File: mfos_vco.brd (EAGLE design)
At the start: 100 x 80.8 mm, 60 parts, among them IC1 TL072P, IC2 TL072P, IC3 TL072P, IC4 LM394N, U1 POWER, U2 2N5457

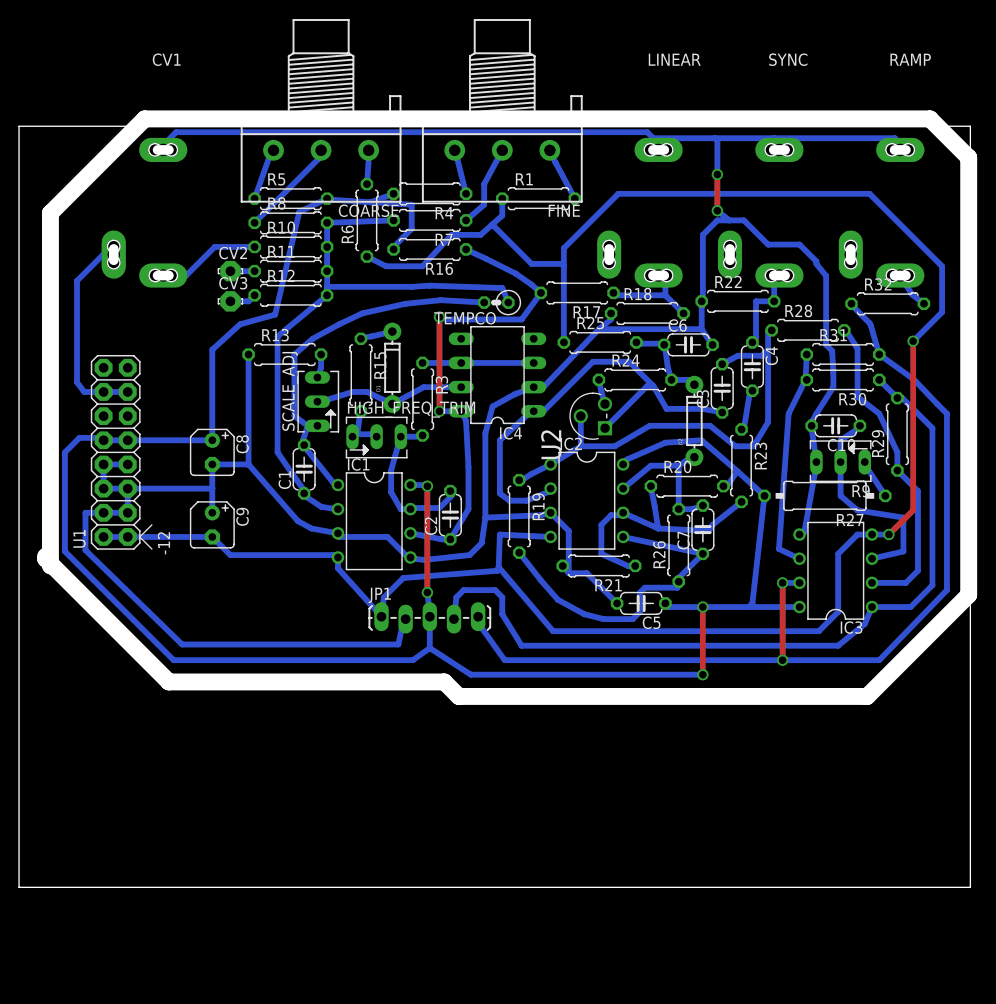
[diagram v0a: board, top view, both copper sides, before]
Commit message: thicker traces and fewer jumps
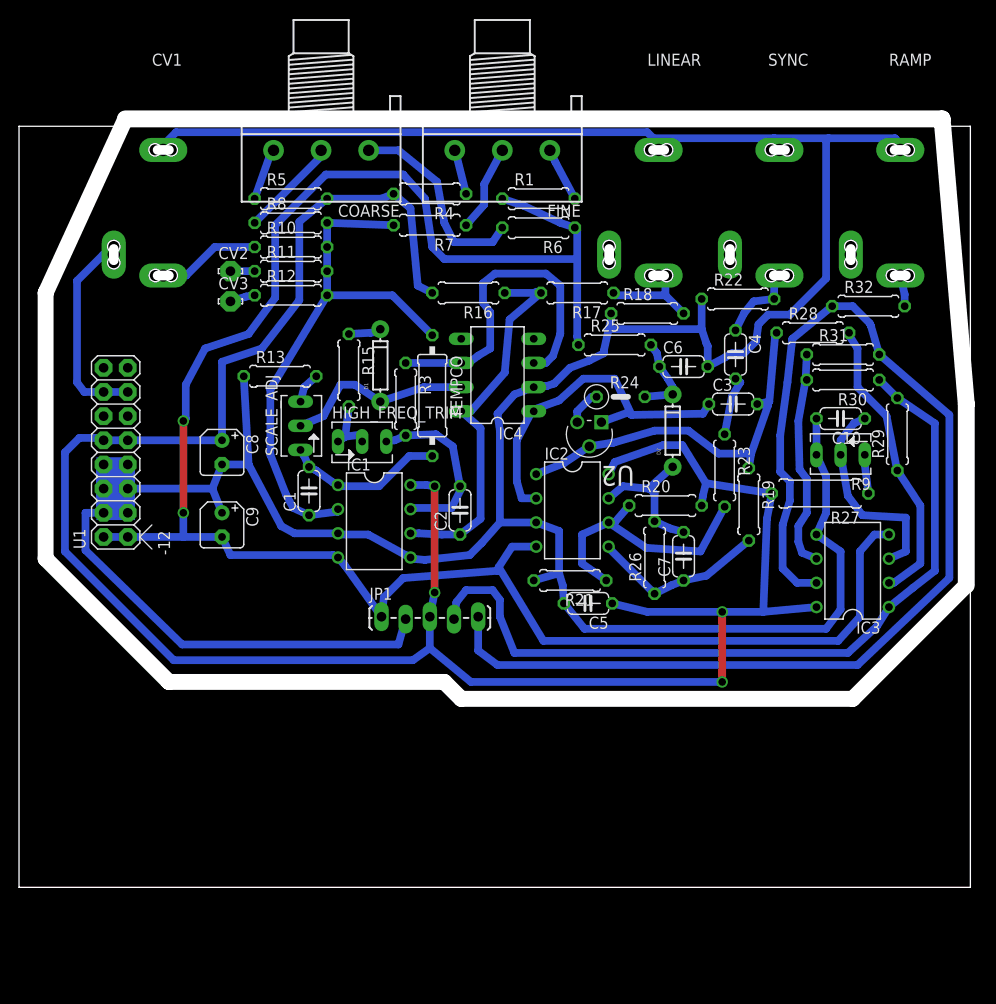
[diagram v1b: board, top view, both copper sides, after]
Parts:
- R24: device rcl:0207/7 -> rcl:0207/5V
- R27: device rcl:0309/12 -> rcl:0309/10
- TEMPCO: device rcl:0207/2V -> rcl:0309/12
- moved R19 24.2 mm to (76.7, 40.3)
- moved R6 18.1 mm to (54.6, 69.3), turned to 180 degrees
- moved TEMPCO 11.9 mm to (43.4, 51.7), turned to 270 degrees
- moved R16 6.12 mm to (47.2, 62.5)
- moved C5 5.59 mm to (59.8, 29.8)
- moved U2 4.46 mm to (58.7, 46.4), turned to 180 degrees
- moved C7 3.45 mm to (69.8, 34.8)
- moved R21 3.41 mm to (57.9, 32.3)
- moved SCALE_ADJ 3.10 mm to (29.6, 48.5)
- moved R20 3.06 mm to (67.9, 40.1)
- moved R26 2.84 mm to (66.8, 34.7)
- moved D2 2.50 mm to (68.7, 48.0)
- moved C6 2.34 mm to (69.8, 54.7)
- moved R13 2.34 mm to (27.4, 53.7)
- moved C1 2.34 mm to (30.5, 41.7)
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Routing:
- net N$35: track 99.2 -> 126.6 mm, vias 2 -> 0
- net N$12: track 11.7 -> 36.3 mm
- net N$9: track 38.3 -> 16.9 mm
- net GND: track 332.1 -> 350.7 mm, vias 2 -> 0
- net N$1: track 3.65 -> 20.9 mm
- net +12V: track 220.4 -> 237.6 mm
- net N$22: track 35.2 -> 18.5 mm
- net -12V: track 222.9 -> 206.4 mm
- net N$13: track 51.8 -> 40.8 mm, vias 2 -> 0
- net N$23: track 48.3 -> 37.5 mm
- net N$21: track 48.8 -> 41.8 mm
- net N$10: track 62.9 -> 57.4 mm
- net N$8: track 16.0 -> 19.9 mm
- net N$31: track 33.6 -> 31.3 mm
- net N$24: track 4.43 -> 6.41 mm
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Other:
- outline, holes or cut-outs redrawn

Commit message: molex
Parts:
- removed C8, C9: 10uF, rcl:B45181A
- removed JP1: (no value), SparkFun-Connectors:1X05_LOCK_LONGPADS
- removed U1: POWER, eurorack:POWER_16
- added C11, C12: 10u, rcl:B45181A
- added C13, C14: 100n, rcl:C050-024X044
- added PWR1: POWER, eurorack:POWER_16
- added U$1, U$2: FB, adafruit:FB
- added X1: 22-23-2051, con-molex:22-23-2051
- CV2, CV3: value LSP10 -> 22-23-2021; device solpad:LSP10 -> con-molex:22-23-2021
- R26: device rcl:0207/7 -> rcl:0309/10
- R27: device rcl:0309/10 -> rcl:0207/10
- moved CV1 115.0 mm to (93.7, 1.02), turned to 180 degrees
- moved RAMP 106.5 mm to (16.3, 1.02), turned to 180 degrees
- moved SYNC 91.4 mm to (29.0, 1.02), turned to 180 degrees
- moved R32 85.3 mm to (14.6, 19.9), turned to 180 degrees
- moved COARSE 84.2 mm to (72.1, 3.56), turned to 0 degrees
- moved R29 82.0 mm to (11.6, 33.4), turned to 270 degrees
- moved LINEAR 81.6 mm to (41.7, 1.02), turned to 180 degrees
- moved R5 79.0 mm to (75.3, 8.64), turned to 180 degrees
- moved R31 76.0 mm to (17.3, 25.0), turned to 180 degrees
- moved R8 75.0 mm to (75.3, 11.2), turned to 180 degrees
- moved FINE 73.9 mm to (53.1, 3.56), turned to 0 degrees
- moved R30 73.9 mm to (17.3, 27.7), turned to 0 degrees
- moved CV2 73.5 mm to (82.5, 22.9), turned to 90 degrees
- moved IC3 72.8 mm to (16.3, 47.8), turned to 270 degrees
- moved R28 72.3 mm to (20.4, 22.7), turned to 180 degrees
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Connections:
- new net N$38: PWR1.10, PWR1.9, U$1.P$1
- new net N$39: PWR1.1, PWR1.2, U$2.P$1
- net +12V: now also C11.+, C13.1, U$1.P$2, X1.3; no longer C8.+, JP1.3, U1.10, U1.9
- net -12V: now also C12.-, C14.2, U$2.P$2, X1.1; no longer C9.-, JP1.1, U1.1, U1.2
- net GND: now also CV2.2, CV3.2, X1.2; no longer C8.-, C9.+, JP1.2, U1.3, U1.4, U1.5, U1.6, U1.7, U1.8
- net N$11: now also PWR1.13, PWR1.14; no longer U1.13, U1.14
- net N$18: now also CV2.1; no longer CV2.MP
- net N$19: now also CV3.1; no longer CV3.MP
- net N$26: now also C11.-, C12.+, C13.2, C14.1, PWR1.3, PWR1.4, PWR1.5, PWR1.6, PWR1.7, PWR1.8
- net N$33: now also X1.4; no longer JP1.4
- net N$35: now also X1.5; no longer JP1.5
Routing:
- net GND: track 350.7 -> 0.00 mm
- net +12V: track 237.6 -> 0.00 mm, vias 4 -> 0
- net -12V: track 206.4 -> 0.00 mm, vias 2 -> 0
- net N$35: track 126.6 -> 0.00 mm
- net N$33: track 84.2 -> 0.00 mm
- net N$10: track 57.4 -> 0.00 mm
- net N$21: track 41.8 -> 0.00 mm
- net N$40: track 40.8 -> 0.00 mm
- net N$23: track 37.5 -> 0.00 mm
- net N$12: track 36.3 -> 0.00 mm
- net N$31: track 31.3 -> 0.00 mm
- net N$26: track 28.0 -> 0.00 mm
- net N$34: track 23.3 -> 0.00 mm
- net N$28: track 22.0 -> 0.00 mm
- net N$11: track 21.5 -> 0.00 mm
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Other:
- board size 100 x 80.8 mm -> 100 x 80 mm

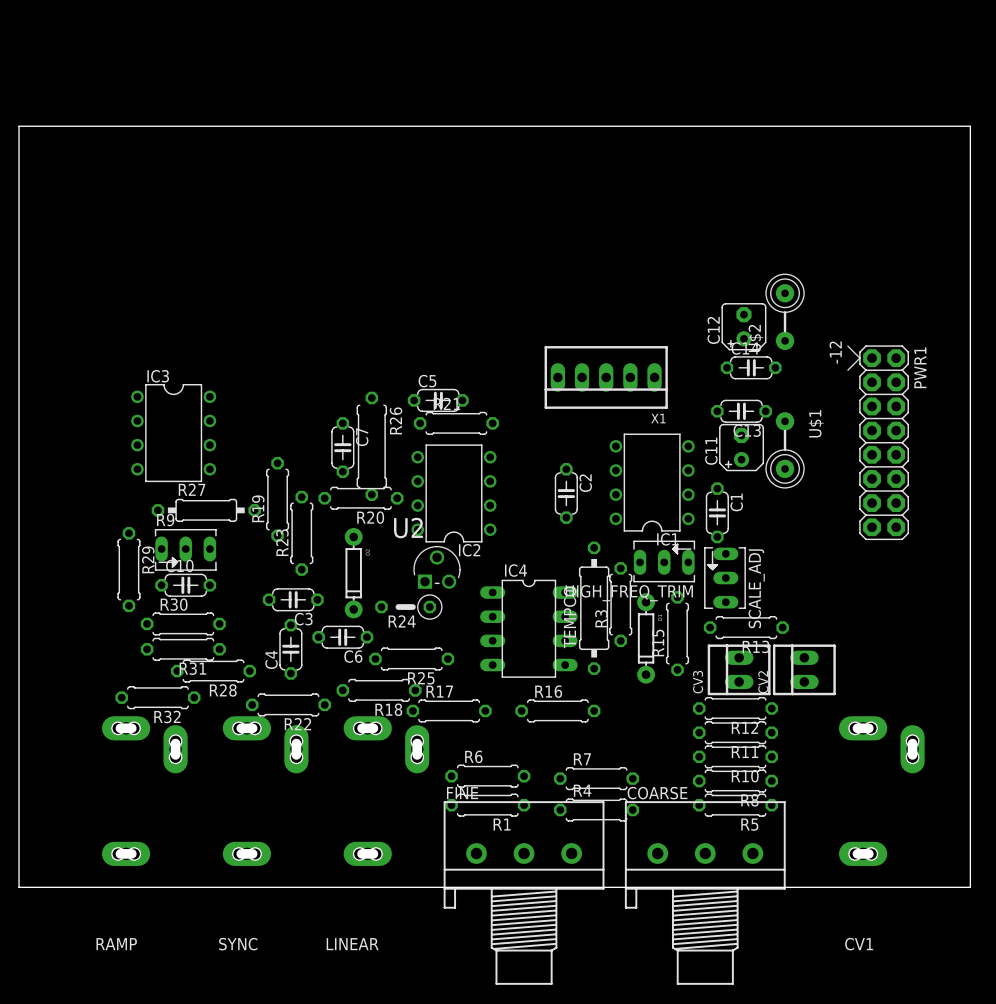
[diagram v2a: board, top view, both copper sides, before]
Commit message: corrected separate ground signals and manually routed
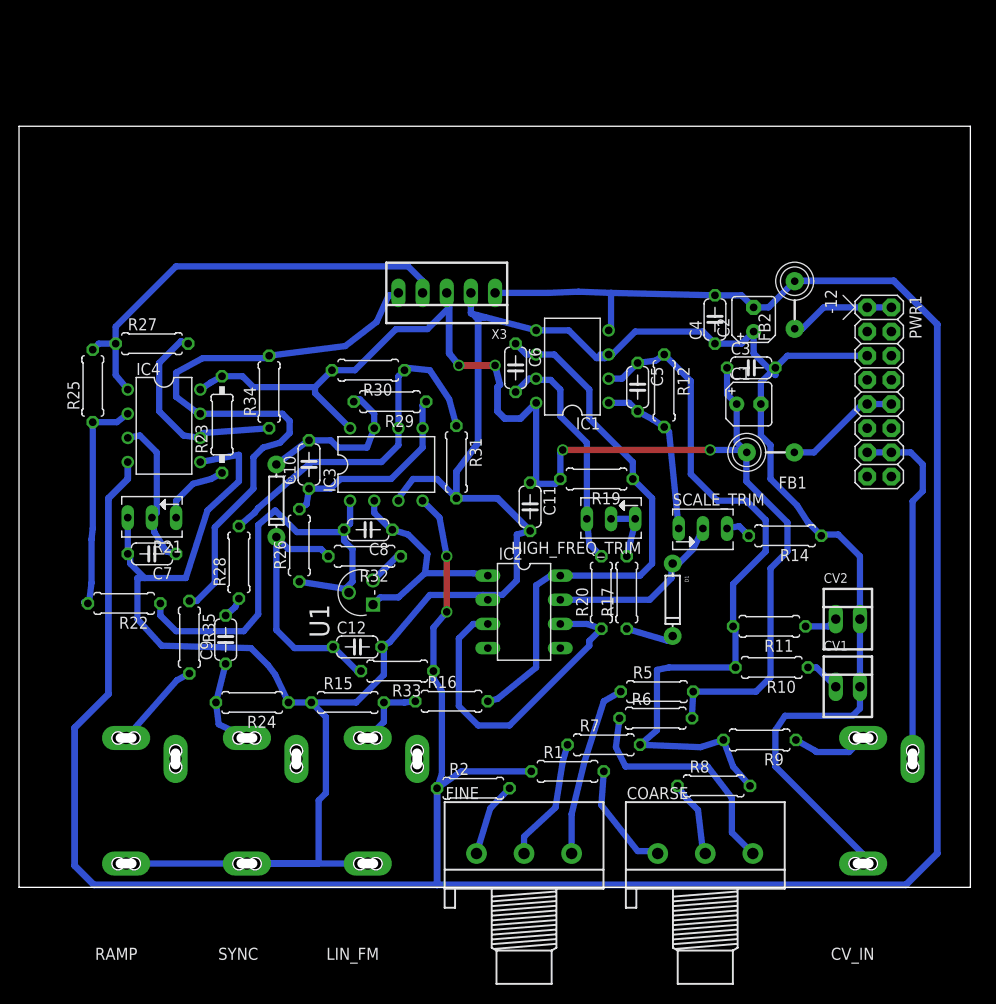
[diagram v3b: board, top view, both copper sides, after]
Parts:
- removed C13, C14: 100n, rcl:C050-024X044
- removed CV3: 22-23-2021, con-molex:22-23-2021
- removed LINEAR: AUDIO-JACK, erthenvar:ERTHENVAR-JACK-90DEG
- removed R13: 475, rcl:0207/7
- removed R18: 100k, rcl:0207/7
- removed R3: 10k, rcl:0207/7
- removed R4: 200k, rcl:0207/7
- removed SCALE_ADJ: 100R, pot:B64Y
- removed TEMPCO: 2k, rcl:0309/12
- removed U$1, U$2: FB, adafruit:FB
- removed U2: 2N5457, Fairchild_By_element14_Batch_1:TO127P254X732-3
- removed X1: 22-23-2051, con-molex:22-23-2051
- added C8: .005uF, rcl:C050-024X044
- added C9: .001uF, rcl:C050-024X044
- added CV_IN, LIN_FM: AUDIO-JACK, erthenvar:ERTHENVAR-JACK-90DEG
- added FB1, FB2: FB, adafruit:FB
- added R14: 475, rcl:0207/7
- added R2: 200k, rcl:0207/7
- added R33: 18k, rcl:0207/7
- added R34: 10k, rcl:0207/7
- added R35: 1k, rcl:0207/7
- added SCALE_TRIM: 100R, pot:B64Y
- added U1: 2N5457, Fairchild_By_element14_Batch_1:TO127P254X732-3
- added X3: 22-23-2051, con-molex:22-23-2051
- C1, C2: value 100pF -> 10u; device rcl:C050-024X044 -> rcl:B45181A
- C10: value 0.1uF -> 4p7F
- C11: value 10u -> 0.1uF; device rcl:B45181A -> rcl:C050-024X044
- C12: value 10u -> 100pF; device rcl:B45181A -> rcl:C050-024X044
- C3: value .005uF -> 100n
- C4: value .001uF -> 100n
- C5: value 0.1uF -> 100pF
- C7: value 4p7F -> 0.1uF
- CV1: value AUDIO-JACK -> 22-23-2021; device erthenvar:ERTHENVAR-JACK-90DEG -> con-molex:22-23-2021
- IC2: value TL072P -> LM394N; device linear:DIL08 -> synthdiy:DIL08
- IC4: value LM394N -> TL072P; device synthdiy:DIL08 -> linear:DIL08
- R1: value 200k -> 10k
- R12: value 100k -> 2k
- R15: value 4k7 -> 100k
- R17: value 1M -> 4k7
- R19: value 10k -> 1M
- R21: value 2k -> 10k; device rcl:0207/7 -> pot:B64Y
- R22: value 100k -> 10k
- R23: value 1k -> 100k; device rcl:0207/7 -> rcl:0207/10
- R24: device rcl:0207/5V -> rcl:0207/7
- R25: value 18k -> 47k
- R26: value 1M -> 10k; device rcl:0309/10 -> rcl:0207/7
- R27: value 100k -> 10k; device rcl:0207/10 -> rcl:0207/7
- R28: value 10k -> 1k
- R29: value 47k -> 1M
- R31: value 10k -> 2k
- R32: value 1k -> 100k
- R5: value 47k -> 200k
- R6: value 10k -> 47k
- R9: value 10k -> 100k; device pot:B64Y -> rcl:0207/7
- moved R9 63.6 mm to (77.9, 15.5), turned to 180 degrees
- moved C4 56.5 mm to (73.2, 59.7)
- moved C3 54.0 mm to (77.0, 54.6), turned to 0 degrees
- moved C12 52.8 mm to (35.6, 25.3), turned to 0 degrees
- moved R25 44.1 mm to (7.75, 52.7), turned to 90 degrees
- moved IC4 43.9 mm to (15.2, 48.5)
- moved R15 35.4 mm to (34.5, 19.4), turned to 0 degrees
- moved R31 34.8 mm to (46.0, 44.7), turned to 270 degrees
- moved R12 34.2 mm to (67.8, 52.2), turned to 270 degrees
- moved C6 33.6 mm to (52.2, 54.6), turned to 270 degrees
- moved R19 33.6 mm to (60.7, 42.9), turned to 180 degrees
- moved R21 33.5 mm to (14.0, 38.9), turned to 180 degrees
- moved R30 33.0 mm to (36.7, 54.4), turned to 180 degrees
- moved R29 32.6 mm to (39.0, 51.1), turned to 180 degrees
- moved R20 27.1 mm to (61.2, 31.0), turned to 90 degrees
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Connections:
- removed net N$19 (its old number): CV3.1, R12.1
- new net N$18: CV1.1, R10.1
- net +12V: now also C1.+, C11.1, C3.1, FB1.P$2, IC4.8, R19.2, R23.2, R30.2, R6.2, X3.3; no longer C11.+, C13.1, C5.1, IC2.8, R16.2, R20.2, R27.2, R4.2, U$1.P$2, X1.3
- net -12V: now also C2.-, C4.2, FB2.P$2, IC4.4, R2.1, R33.1, X3.1; no longer C12.-, C14.2, IC2.4, R25.1, R6.1, U$2.P$2, X1.1
- net GND: now also C1.-, C11.2, C12.2, C2.+, C3.2, C4.1, C7.2, CV1.2, CV_IN.P$1, IC2.2, IC3.3, IC4.5, LIN_FM.P$1, PWR1.3, PWR1.4, PWR1.5, PWR1.6, PWR1.7, PWR1.8, R14.1, R15.1, R21.A, R24.1, R31.2, X3.2; no longer C10.2, C5.2, C6.2, CV1.P$1, CV3.2, IC2.3, IC3.5, IC4.2, LINEAR.P$1, R13.1, R18.1, R21.2, R22.1, R9.A, X1.2
- net N$1: now also R1.2; no longer R6.2
- net N$10: now also C5.1, R12.1, R9.2; no longer C1.1, R12.2, TEMPCO.1
- net N$11: now also CV_IN.P$2; no longer CV1.P$2
- net N$12: now also IC2.3, IC2.6, R20.1; no longer IC4.3, IC4.6, R3.1
- net N$14: now also R17.2; no longer R15.2
- net N$15: now also R17.1; no longer R15.1
- net N$16: now also C6.2, R20.2; no longer C2.2, R3.2
- net N$17: now also CV_IN.P$3, R9.1; no longer CV1.P$3, R10.1
- net N$2: now also R2.2; no longer R1.2
- net N$20: now also LIN_FM.P$3, R15.2, R16.1; no longer LINEAR.P$3, R17.1, R18.2
- net N$21: now also C8.2, IC3.1, R22.1, R26.1, U1.2; no longer C3.2, IC2.1, R19.1, R28.1, U2.2
- net N$22: now also C10.1, IC3.5, R26.2, R29.1; no longer C7.1, IC2.5, R19.2, R26.1
- net N$23: now also C8.1, IC2.1, IC3.2, U1.1; no longer C3.1, IC2.2, IC4.1, U2.1
- net N$24: now also C9.2, R28.1; no longer C4.2, R23.1
- net N$25: now also C9.1, R24.2; no longer C4.1, R22.2
- net N$26: now also IC3.6, R28.2, R30.1, R31.1; no longer C11.-, C12.+, C13.2, C14.1, IC2.6, PWR1.3, PWR1.4, PWR1.5, PWR1.6, PWR1.7, PWR1.8, R20.1, R21.1, R23.2
- net N$27: now also R21.E, R23.1; no longer R27.1, R9.E
- net N$28: now also C7.1, IC4.3, R21.S; no longer C10.1, IC3.3, R9.S
- net N$29: now also R32.1, U1.3; no longer R24.1, U2.3
- net N$3: now also R5.1; no longer R4.1
- net N$30: now also C10.2, IC3.7, R29.2; no longer C7.2, IC2.7, R26.2
- net N$31: now also IC4.2, R22.2, R25.1; no longer IC3.2, R28.2, R29.1
- net N$32: now also C12.1, R32.2, R33.2; no longer C6.1, R24.2, R25.2
- net N$33: now also IC4.1, R25.2, R27.1, X3.4; no longer IC3.1, R29.2, R30.1, X1.4
- net N$34: now also IC4.6, R27.2, R34.1; no longer IC3.6, R30.2, R31.1
- net N$35: now also IC4.7, R34.2, R35.1, X3.5; no longer IC3.7, R31.2, R32.1, X1.5
- net N$36: now also R35.2; no longer R32.2
- net N$38: now also FB1.P$1; no longer U$1.P$1
- net N$39: now also FB2.P$1; no longer U$2.P$1
- net N$4: now also R6.1; no longer R5.1
- net N$40: now also C6.1, IC2.8, R16.2, R19.1; no longer C2.1, IC4.8, R16.1, R17.2
- net N$7: now also R14.2, SCALE_TRIM.A; no longer R13.2, SCALE_ADJ.A
- net N$8: now also IC2.7, SCALE_TRIM.S; no longer IC4.7, SCALE_ADJ.S
- net N$9: now also C5.2, R12.2, SCALE_TRIM.E; no longer C1.2, SCALE_ADJ.E, TEMPCO.2
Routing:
- net GND: track 0.00 -> 307.6 mm
- net -12V: track 0.00 -> 299.9 mm, vias 0 -> 2
- net +12V: track 0.00 -> 140.4 mm, vias 0 -> 4
- net N$10: track 0.00 -> 78.9 mm
- net N$35: track 0.00 -> 66.5 mm
- net N$40: track 0.00 -> 58.7 mm
- net N$21: track 0.00 -> 48.7 mm
- net N$33: track 0.00 -> 46.5 mm
- net N$11: track 0.00 -> 37.8 mm
- net N$26: track 0.00 -> 37.5 mm
- net N$12: track 0.00 -> 35.5 mm
- net N$32: track 0.00 -> 26.9 mm
- net N$16: track 0.00 -> 25.0 mm
- net N$4: track 0.00 -> 24.9 mm
- net N$23: track 0.00 -> 23.9 mm
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
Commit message: routed manually with two jumpers
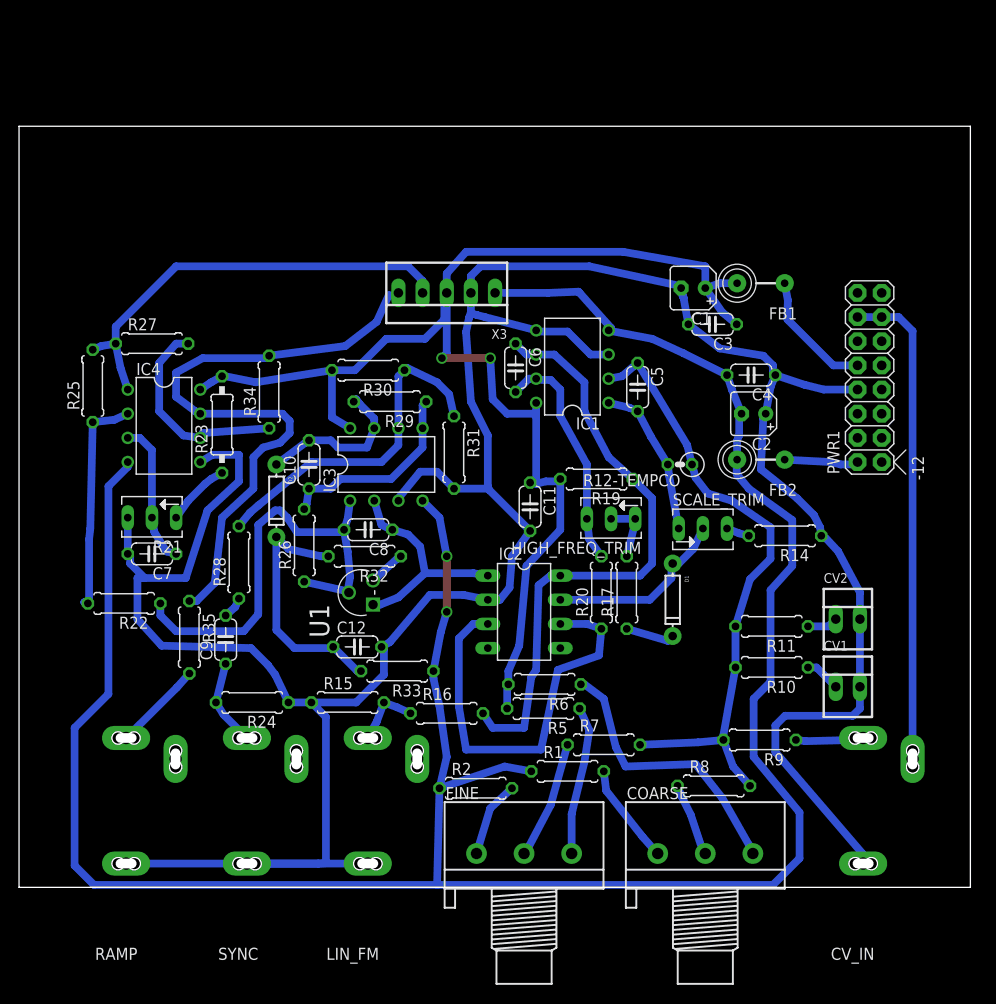
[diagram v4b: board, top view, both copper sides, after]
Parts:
- removed R12: 2k, rcl:0207/7
- added R12-TEMPCO: 2k, rcl:0207/2V
- moved FB1 17.8 mm to (78.0, 63.5)
- moved FB2 16.6 mm to (78.0, 45.0), turned to 180 degrees
- moved C1 13.5 mm to (70.9, 63.0), turned to 180 degrees
- moved R6 12.2 mm to (55.2, 21.3), turned to 180 degrees
- moved R5 12.1 mm to (55.1, 18.8), turned to 180 degrees
- moved C2 9.91 mm to (77.2, 49.8), turned to 180 degrees
- moved C4 6.97 mm to (77.0, 53.8), turned to 180 degrees
- moved C3 6.12 mm to (72.9, 59.2), turned to 180 degrees
- moved PWR1 3.70 mm to (89.4, 51.1), turned to 90 degrees
- moved R16 1.37 mm to (45.0, 18.3)
- moved R31 1.05 mm to (45.7, 45.7)
- moved R26 0.51 mm to (30.0, 35.9)
- moved R2 0.25 mm to (48.0, 10.4)
- moved R11 0.25 mm to (79.1, 27.4)
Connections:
- net N$10: now also R12-TEMPCO.1; no longer R12.1
- net N$9: now also R12-TEMPCO.2; no longer R12.2
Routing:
- net -12V: track 299.9 -> 260.2 mm
- net N$10: track 78.9 -> 64.9 mm
- net N$11: track 37.8 -> 51.4 mm
- net GND: track 307.6 -> 317.8 mm
- net N$12: track 35.5 -> 43.7 mm
- net N$40: track 58.7 -> 63.7 mm
- net N$4: track 24.9 -> 29.0 mm
- net N$39: track 11.1 -> 7.80 mm
- net N$3: track 18.5 -> 15.7 mm
- net N$1: track 11.9 -> 10.6 mm
- net N$26: track 37.5 -> 36.2 mm
- net N$9: track 17.6 -> 16.4 mm
- net +12V: track 140.4 -> 139.3 mm, vias 4 -> 2
- net N$21: track 48.7 -> 47.8 mm
- net N$38: track 12.3 -> 13.2 mm
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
